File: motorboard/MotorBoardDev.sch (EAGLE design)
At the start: 88 parts, among them IC1 74HC04D, J1 Under Glow, J2 Safety Light, J3 12V, J4 24V, Q1 BC846ASMD, Q2 220mA/50V/3.5Ω, Q7 220mA/50V/3.5Ω, Q8 220mA/50V/3.5Ω, Q9 220mA/50V/3.5Ω, T11 TIP41A, T12 TIP41A, T13 TIP41A, T14 TIP41A, T15 TIP41A, T16 TIP41A, T17 TIP41A, T18 TIP41A, T19 TIP41A, T2 TIP41A, U2 9DoF IMU, X1 C-GRID-05-15-91, X2 C-GRID-05-15-91, X4 C-GRID-02-70553, X5 SI-50170, X7 2510-, X8 2510-

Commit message: restructuring
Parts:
- removed D10: WHITE, SparkFun-LED:LED0603
- removed D11, D12: 3.3V, SparkFun-DiscreteSemi:DIODE-ZENER-MM3Z3V3T1G
- removed D7: RED, SparkFun-LED:LED0603
- removed D8: BLUE, SparkFun-LED:LED0603
- removed D9: GREEN, SparkFun-LED:LED0603
- removed IC1: 74HC04D, 74xx-eu:74HC04D
- removed R20: 200, SparkFun-Resistors:200OHM-0603-1/10W-1%
- removed R26, R30: 2700, SparkFun-Resistors:3.9KOHM-0603-1/10W-1%
- removed T11, T12, T13, T14, T15, T16, T17, T18, T19: TIP41A, transistor:-PNP-TO220V
- removed U$15: MBED1768, SparkFun-Boards:MBED_NXP_LPC1768
- removed U$7: NCP1117DT50GOS-ND, IGVC-Regulators:NCP1117DT50GOS-ND
- removed U$8: NCP1117DT33GOS-ND, IGVC-Regulators:NCP1117DT33GOS-ND
- added A1: MBED1768, MotorBoardDev:SPARKFUN-BOARDS_MBED_NXP_LPC1768
- added D1, D2: GREEN, SparkFun-LED:LED-GREEN0603
- added D3: WHITE, SparkFun-LED:LED-WHITE0603
- added D4: BLUE, SparkFun-LED:LED-BLUE0603
- added FQP30N06L, Q15, Q16: TIP41C, transistor-power:TIP41C
- added Q10, Q11, Q3, Q4, Q5, Q6: TIP42C, transistor-power:TIP42C
- added T1: NCP1117DT50GOS-ND, IGVC-Regulators:NCP1117DT50GOS-ND
- added T3: NCP1117DT33GOS-ND, IGVC-Regulators:NCP1117DT33GOS-ND
- added X3: MINI-USB_SHIELD5P4-32005-400, con-cypressindustries:MINI-USB_SHIELD5P4-32005-400
- C1: device SparkFun-Capacitors:0.1UF-0603-25V-(+80/-20%) -> SparkFun-Capacitors:0.1UF-0603-100V-10%
- C11, C12, C13, C14: value (none) -> 10uF
- Q1: value BC846ASMD -> TIP42C; device transistor-npn:BC846ASMD -> transistor-power:TIP42C
- R10: value 2700 -> 200; device SparkFun-Resistors:3.9KOHM-0603-1/10W-1% -> SparkFun-Resistors:200OHM-0603-1/10W-1%
- R16: value 536 -> 200; device SparkFun-Resistors:3.9KOHM-0603-1/10W-1% -> SparkFun-Resistors:200OHM-0603-1/10W-1%
- R18, R19: value 200 -> 4.7k; device SparkFun-Resistors:200OHM-0603-1/10W-1% -> SparkFun-Resistors:4.7KOHM-0603-1/10W-1%
- R39, R40: value 150 -> 500; device rcl:R-US_R0603 -> SparkFun-Resistors:1KOHM-0603-1/10W-1%
- R7: value 200 -> 50
- R8: value 2700 -> 1800; device SparkFun-Resistors:3.9KOHM-0603-1/10W-1% -> SparkFun-Resistors:200OHM-0603-1/10W-1%
- R9: value 2700 -> 1000; device SparkFun-Resistors:3.9KOHM-0603-1/10W-1% -> SparkFun-Resistors:200OHM-0603-1/10W-1%
- T2: device transistor:-NPN-TO220V -> transistor:-PNP-TO220V
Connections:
- removed net !LDIR!: IC1C.O, R23.1
- removed net !LSPEED!: IC1D.O, R21.1
- removed net !RDIR!: IC1B.O, R24.1
- removed net !RSPEED!: IC1A.O, R22.1
- removed net N$24: D9.A, Q1.C, R17.1
- removed net N$33: D9.C, R7.2
- removed net N$34: D8.A, R10.1
- removed net N$35: D10.A, R9.1
- removed net N$7: D7.A, R8.1
- removed net SLIGHT: T2.B, U$15.P$25
- new net BLUE_OUT: J1.1, Q15.E
- new net D+: A1.P$31, X3G$1.3
- new net D-: A1.P$32, X3G$1.2
- new net GREEN_OUT: J1.2, Q16.E
- new net ID: X3G$1.4
- new net INDICATOR_LED: A1.P$8
- new net N$12: D4.A, R9.1
- new net N$5: D1.A, R5.1
- new net N$8: Q11.E, R17.1, X4-1.S
- new net RED_OUT: FQP30N06L.E, J1.3
- new net SAFETY_LIGHT: A1.P$19, T2.B
- net +12V: now also FQP30N06L.C, Q15.C, Q16.C, R17.2, R9.2, T1.IN, T3.IN; no longer R18.2, R19.2, R20.2, T11.E, T17.E, T19.E, U$7.IN, U$8.IN
- net +24V: now also R8.2; no longer D11.C, D12.C, R17.2, R30.2
- net +3V3: now also A1.P$40, R18.2, R19.2, R7.2, T3.OUT; no longer R9.2, U$8.OUT
- net +5V: now also A1.P$2, A1.P$39, R5.2, T1.OUT, X3G$1.1; no longer IC1P.VCC, U$15.P$2, U$7.OUT
- net 1S1: now also A1.P$18; no longer U$15.P$28
- net 1S1O: now also J1.7, Q1.E; no longer J1.4, T12.E
- net 1S2: now also A1.P$17; no longer U$15.P$27
- net 1S2O: now also J1.6, Q4.E; no longer J1.5, T14.E
- net 1S3: now also A1.P$16; no longer U$15.P$26
- net 1S3O: now also J1.5, Q6.E; no longer J1.6, T16.E
- net 2S1: now also A1.P$7; no longer U$15.P$5
- net 2S1O: now also Q3.E; no longer T13.E
- net 2S2: now also A1.P$6; no longer U$15.P$6
- net 2S2O: now also Q5.E; no longer T15.E
- net 2S3: now also A1.P$5; no longer U$15.P$7
- net 2S3O: now also Q10.E; no longer T18.E
- net BATTIN: now also A1.P$20, R10.1; no longer R30.1, U$15.P$20
- net BLUE: now also A1.P$21; no longer J1.1
- net ESTOP: now also A1.P$24, Q11.B; no longer R26.2, X4-1.S, X4-2.S
- net GND: now also A1.P$1, D1.C, D2.C, D3.C, D4.C, J1.4, J1.8, J1.9, J2.2, Q1.C, Q10.C, Q11.C, Q3.C, Q4.C, Q5.C, Q6.C, T1.GND, T2.C, T3.GND, X3G$1.5, X4-2.S; no longer D10.C, D7.C, D8.C, IC1P.GND, Q1.E, R26.1, R5.1, R7.1, T11.C, T12.C, T13.C, T14.C, T15.C, T16.C, T17.C, T18.C, T19.C, T2.E, U$15.P$1, U$7.GND, U$8.GND
- net GREEN: now also A1.P$22; no longer J1.2
- net GYRO_INT: now also A1.P$11; no longer U$15.P$14
- net L+12V: now also R28.2; no longer OK3A.COL, OK3B.COL, R28.1
- net LALI: now also OK3A.COL
- net LBLI: now also OK3B.COL, R28.1; no longer R28.2
- net LDIR: now also A1.P$26, R23.1; no longer IC1C.I, U$15.P$17
- net LEA3: now also A1.P$14; no longer U$15.P$24
- net LEB3: now also A1.P$15; no longer U$15.P$23
- net LSPEED: now also A1.P$25, R21.1; no longer IC1D.I, U$15.P$18
- net N$1: now also T2.E; no longer J2.2, T2.C
- net N$10: now also Q16.B; no longer R20.1, T17.B
- net N$11: now also Q6.B; no longer T16.B
- net N$13: now also Q4.B; no longer T14.B
- net N$14: now also Q1.B; no longer T12.B
- net N$15: now also Q3.B; no longer T13.B
- net N$16: now also Q5.B; no longer T15.B
- net N$28: now also Q10.B; no longer T18.B
- net N$3: now also FQP30N06L.B; no longer R18.1, T11.B
- net N$37: now also A1.P$30; no longer U$15.P$30
- net N$38: now also A1.P$29; no longer U$15.P$29
- net N$4: now also Q15.B; no longer R19.1, T19.B
- net N$6: now also D2.A, R7.1; no longer D11.A, R8.2
- net N$9: now also D3.A, R8.1; no longer D12.A, Q1.B, R5.2
- net R+12V: now also R25.2, R27.2; no longer OK4A.COL, OK4B.COL, R25.1, R27.1
- net RALI: now also OK4A.COL, R27.1; no longer R27.2
- net RBLI: now also OK4B.COL, R25.1; no longer R25.2
- net RD+: now also A1.P$35; no longer U$15.P$35
- net RD-: now also A1.P$36; no longer U$15.P$36
- net RDIR: now also A1.P$28, R24.1; no longer IC1B.I, U$15.P$15
- net REA3: now also A1.P$12; no longer U$15.P$22
- net REB3: now also A1.P$13; no longer U$15.P$21
- net RED: now also A1.P$23; no longer J1.3
- net RSPEED: now also A1.P$27, R22.1; no longer IC1A.I, U$15.P$16
- net SCL: now also A1.P$10, R18.1; no longer U$15.P$10
- net SDA: now also A1.P$9, R19.1; no longer U$15.P$9
- net TD+: now also A1.P$33; no longer U$15.P$33
- net TD-: now also A1.P$34; no longer U$15.P$34
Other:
- note added: "Also logical shifters"
- note added: "Change to AZ2940D-3.3 for assurance over power supply"
- note added: "Change to AZ2940D-5.0 for assurance over power supply"
- note added: "FQP27P06"
- note added: "How it works?"
- note added: "I'll update the package when I get the chance, they look exactly in physical layout and schematics tho"
- note added: "I'll update this when I get the chance to make the library"
- note added: "I'm not sure how 1S1O/2S1O stuff works, but I've made then at least looks functional"
- note added: "ID set to floating to identify the board as a slave"
- note added: "Inverter removed, meaning writing 255 will actually cause 0 and the other way around will cause full speed"
- note added: "Look into this"
- note added: "Overkill?"
- note added: "RGB control pin underglow thrown to PWM"
- note added: "The following are P-Channel Logic Level Mosfet, FQP27P06"
- note added: "The inverter is gone"
- note added: "These are actual logic level mosfet that can run on 3.3V, parts number: FQP30N06L"
- note added: "This is a software problem!!"
- note added: "This transistor will be FQP27P06 as well"
- note added: "Will be a connector with horizontal pinout, JST B2PS-VH"
- note added: "all of Speed control thrown to PWM"
- note added: "pull up resistor position changed, it'll no longer short L/R+12V to L/R GND"
- note removed: "Current limiting R"
- note removed: "Inverter Power"
- note removed: "Inverters"
- moved on the sheet: C1, C11, C12, C13, C14, C2, C3, C5, C6, J4, OK3A, OK3B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

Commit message: Magic
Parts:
- removed Q2, Q7, Q8, Q9: 220mA/50V/3.5Ω, SparkFun-DiscreteSemi:MOSFET-NCH-BSS138
- removed R31, R32, R33, R34, R35, R36, R37, R38: 10k, SparkFun-Resistors:10KOHM-0603-1/10W-1%
- added D5: BLUE, SparkFun-LED:LED-BLUE0603
- added U1: TXB0104DR, MotorBoardDev:TXB0104DR
- D3: value WHITE -> Yellow; device SparkFun-LED:LED-WHITE0603 -> SparkFun-LED:LED-YELLOW0603
- R10: value 200 -> 4.7k
- R16: value 200 -> 500
- R21, R22, R23, R24: value 1k -> 30
- R25, R27, R28, R29: value 10k -> 4.7k
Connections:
- net D+ renamed D_P
- net D- renamed D_N
- net RD+ renamed RD_P
- net RD- renamed RD_N
- net TD+ renamed TD_P
- net TD- renamed TD_N
- removed net ID: X3G$1.4
- removed net LSPEED: A1.P$25, R21.1
- removed net N$37: A1.P$30, R39.1
- removed net N$38: A1.P$29, R40.1
- new net LALI_CTRL: A1.P$23, R21.1
- new net LBLI_CTRL: R23.1
- new net N$17: X7-4.KL
- new net N$18: X7-3.KL
- new net N$7: J2.2, T2.E
- new net RALI_CTRL: R22.1
- new net RBLI_CTRL: R24.1
- net +3V3: now also U1.VCCB; no longer Q2.G, Q7.G, Q8.G, Q9.G, R32.2, R33.2, R35.2, R37.2
- net +5V: now also U1.VCCA; no longer R31.2, R34.2, R36.2, R38.2
- net BLUE: no longer A1.P$21
- net ESTOP: now also A1.P$22; no longer A1.P$24
- net GND: now also D5.C, U1.GND, U1.OE; no longer J1.4, J1.8, J1.9, J2.2
- net GREEN: no longer A1.P$22
- net INDICATOR_LED: now also D5.A
- net LDIR: now also A1.P$24; no longer A1.P$26, R23.1
- net LEA: now also U1.A1; no longer Q2.D, R31.1
- net LEA3: now also U1.B1; no longer Q2.S, R32.1
- net LEB: now also U1.A2; no longer Q8.D, R36.1
- net LEB3: now also U1.B2; no longer Q8.S, R37.1
- net N$1: no longer T2.E
- net RDIR: now also A1.P$26; no longer A1.P$28, R24.1
- net REA: now also U1.A3; no longer Q7.D, R34.1
- net REA3: now also U1.B3; no longer Q7.S, R33.1
- net REB: now also U1.A4; no longer Q9.D, R38.1
- net REB3: now also U1.B4; no longer Q9.S, R35.1
- net RED: no longer A1.P$23
- net RSPEED: now also A1.P$25; no longer A1.P$27, R22.1
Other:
- note added: "#S#O control which bar lights up RGB control the color of the entire stripe"
- note added: "(By OSMC Schematics"
- note added: "Add disable"
- note added: "Also make sure this is the chip we want"
- note added: "Bidirectional"
- note added: "Buck converter"
- note added: "Check 30Ω"
- note added: "Check layout package"
- note added: "If have space add Optoisolator for HI lines"
- note added: "Label them on the board"
- note added: "Make them bigger"
- note added: "Power distribution load switch"
- note added: "Put it bak on"
- note added: "RGB are currently not connected to the mbed"
- note added: "Use Neopixels"
- note added: "Use quad-line 12V inverter"
- note added: "also goes for this"
- note added: "do the same for safety light"
- note added: "fix this"
- note added: "get a SMD?"
- note added: "go from 5v to 3v3 not 12V"
- note added: "make absolute voltage 3V"
- note removed: "Also logical shifters"
- note removed: "How it works?"
- note removed: "ID set to floating to identify the board as a slave"
- note removed: "Inverter removed, meaning writing 255 will actually cause 0 and the other way around will cause full speed"
- note removed: "Overkill?"
- note removed: "RGB control pin underglow thrown to PWM"
- note removed: "This is a software problem!!"
- note removed: "all of Speed control thrown to PWM"
- note removed: "pull up resistor position changed, it'll no longer short L/R+12V to L/R GND"
- moved on the sheet: C3, C4, OK3A, OK4A, OK4B, Q15, Q16, R18, R19, R2, R21, R22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

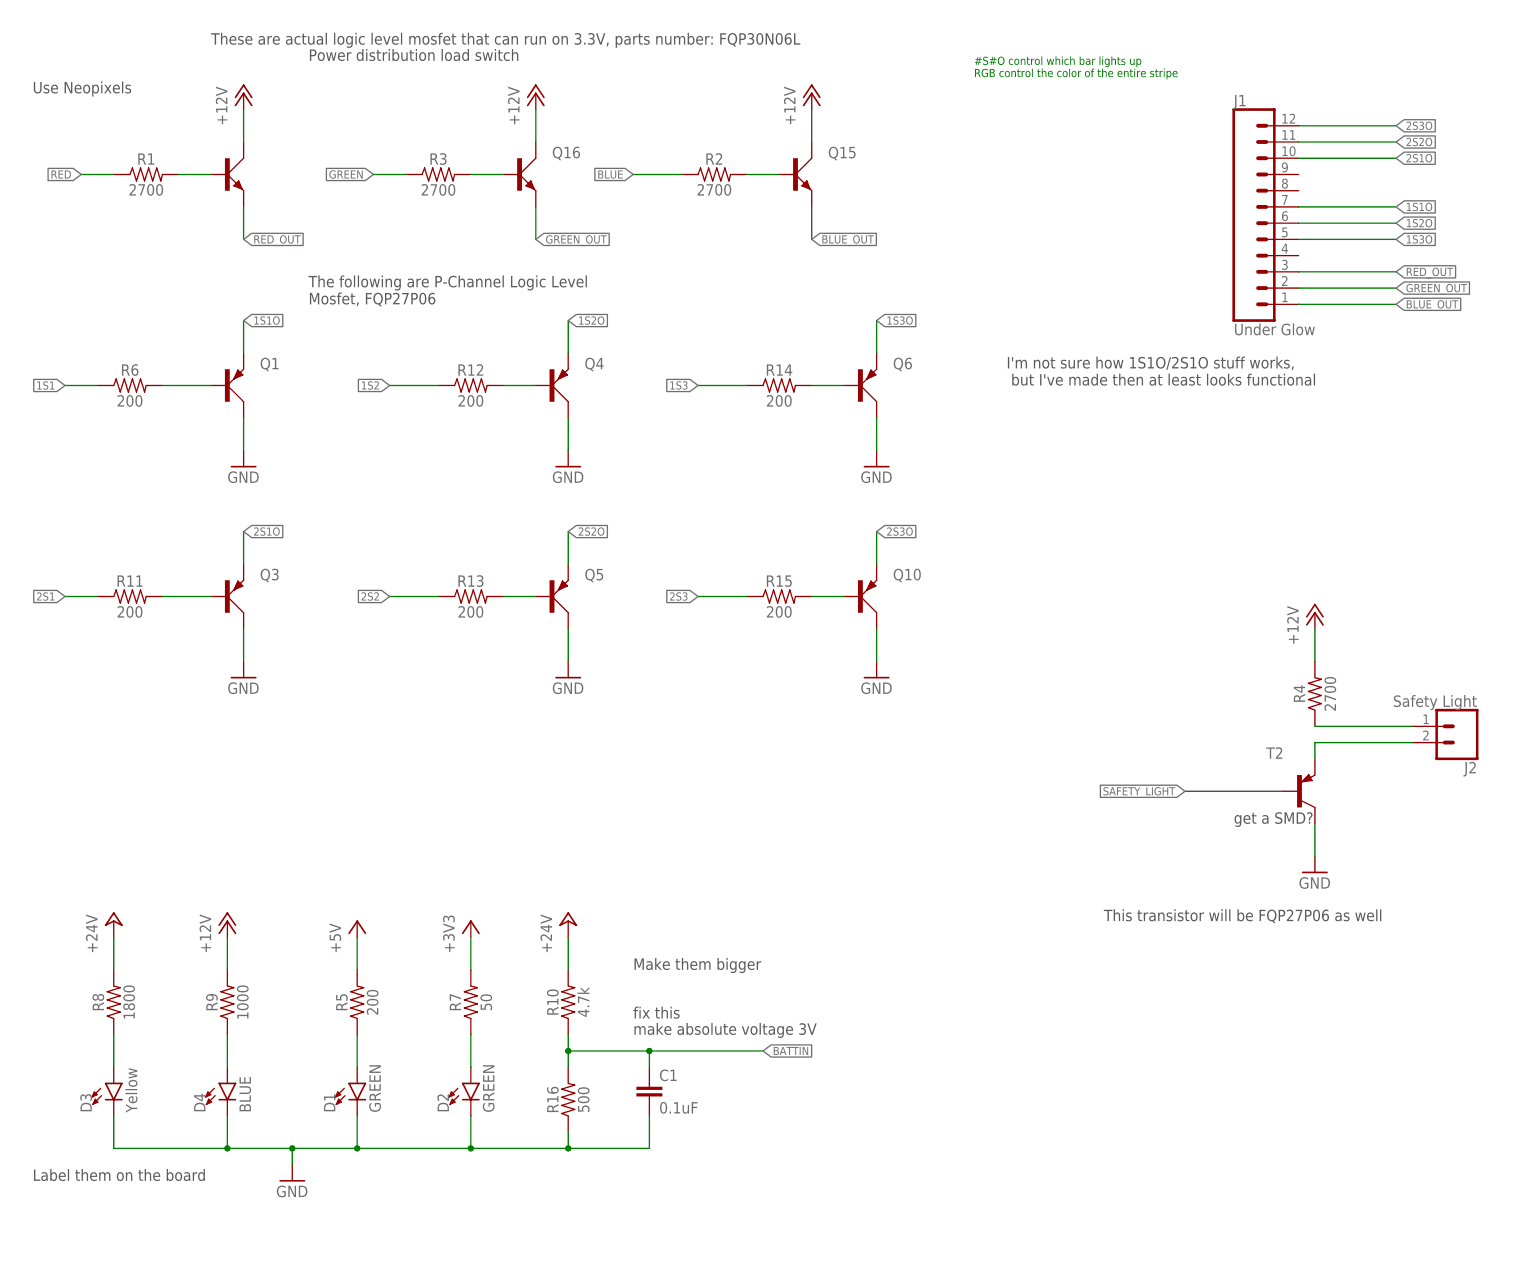
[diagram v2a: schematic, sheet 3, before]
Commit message: Changes so far so Ryan3 can complete BOM
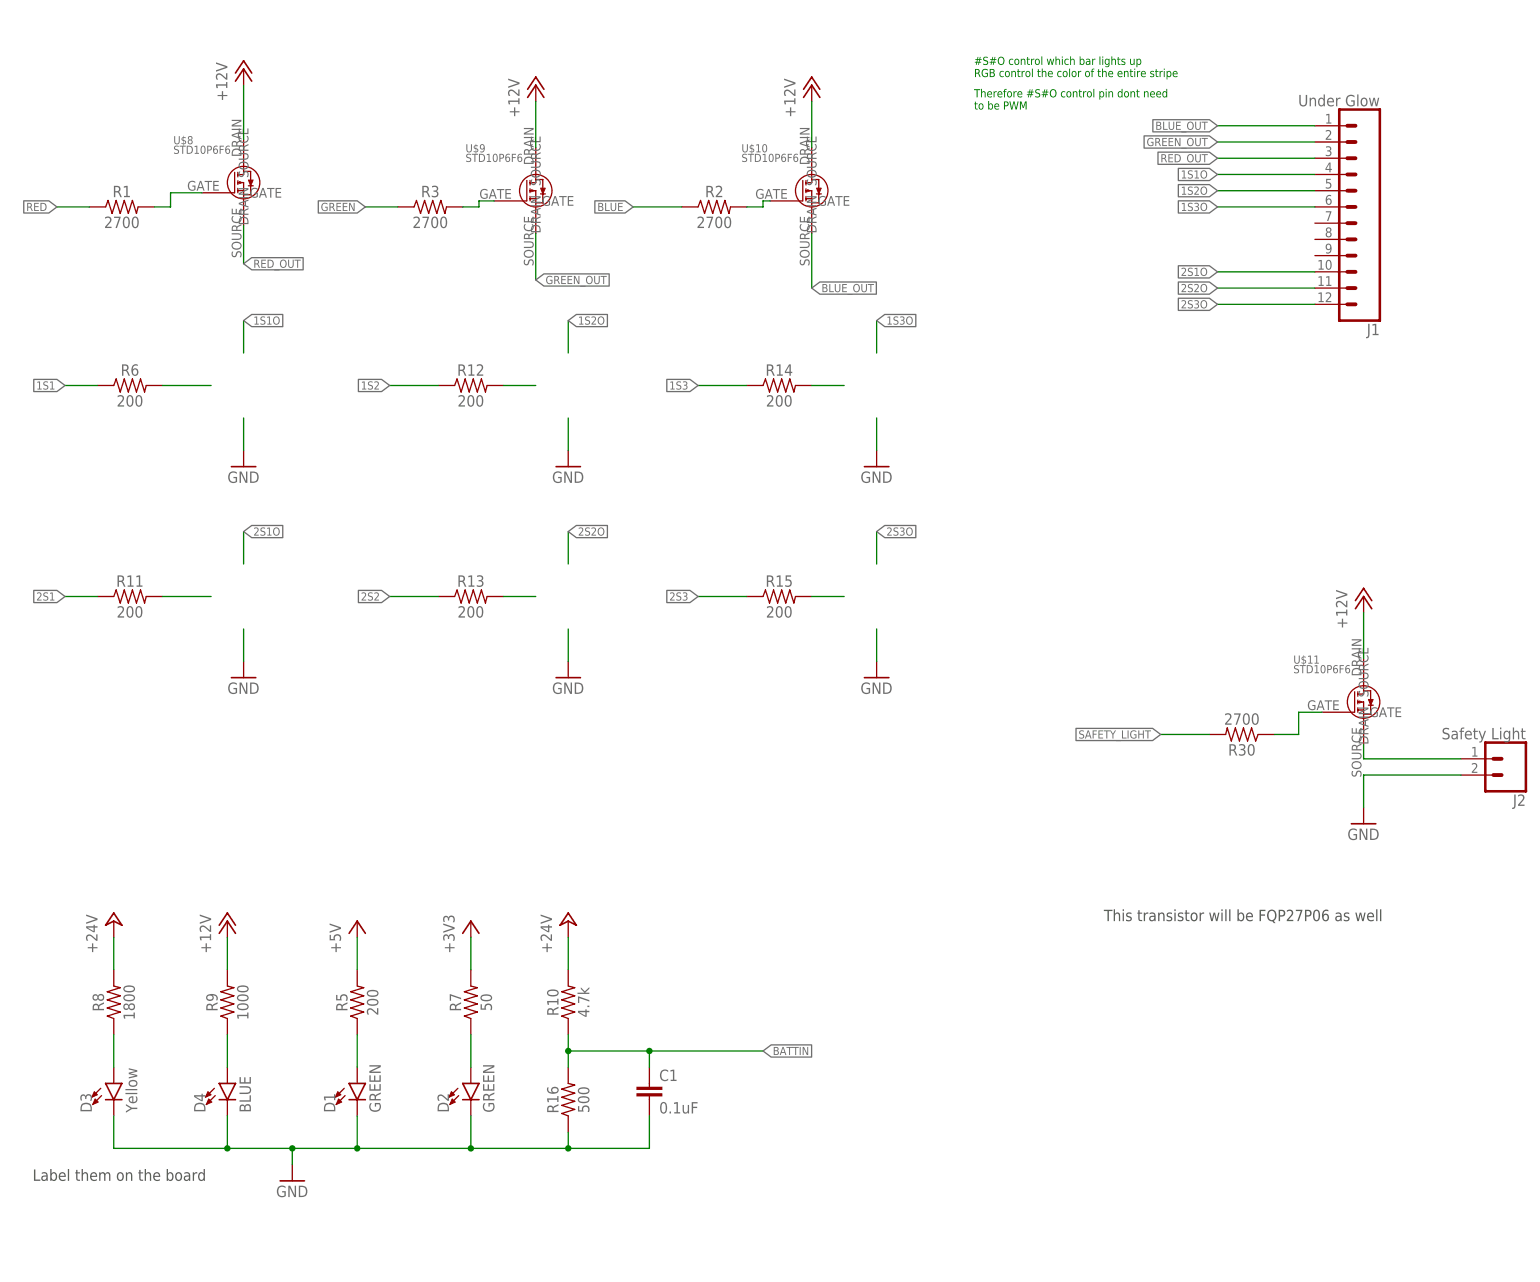
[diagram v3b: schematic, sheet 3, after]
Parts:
- removed FQP30N06L, Q15, Q16: TIP41C, transistor-power:TIP41C
- removed Q1, Q10, Q11, Q3, Q4, Q5, Q6: TIP42C, transistor-power:TIP42C
- removed R17: 2700, SparkFun-Resistors:3.9KOHM-0603-1/10W-1%
- removed T2: TIP41A, transistor:-PNP-TO220V
- added R20, R26: 1k, SparkFun-Resistors:10KOHM-0603-1/10W-1%
- added R30: 2700, SparkFun-Resistors:3.9KOHM-0603-1/10W-1%
- added U$10, U$11, U$12, U$8, U$9: STD10P6F6, MotorBoardDev:STD10P6F6
- added U3, U4: TXB0104DR, MotorBoardDev:TXB0104DR
- R4: value 2700 -> (none); device SparkFun-Resistors:3.9KOHM-0603-1/10W-1% -> rcl:R-US_R0603
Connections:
- removed net LDIR: A1.P$24
- removed net RDIR: A1.P$26
- removed net RSPEED: A1.P$25
- new net LDISABLE: R20.2, X7-4.KL
- new net N$19: R3.2, U$9.GATE
- new net RDISABLE: R26.2, X8-4.KL
- net +12V: now also U$10.DRAIN, U$11.DRAIN, U$12.DRAIN, U$8.DRAIN, U$9.DRAIN; no longer FQP30N06L.C, Q15.C, Q16.C, R17.2, R4.2
- net 1S1O: now also J1.4; no longer J1.7, Q1.E
- net 1S2O: now also J1.5; no longer J1.6, Q4.E
- net 1S3O: now also J1.6; no longer J1.5, Q6.E
- net 2S1O: no longer Q3.E
- net 2S2O: no longer Q5.E
- net 2S3O: no longer Q10.E
- net BLUE: now also A1.P$29
- net BLUE_OUT: now also U$10.SOURCE; no longer Q15.E
- net ESTOP: now also A1.P$27, R4.1; no longer A1.P$22, Q11.B
- net GND: now also J2.2; no longer Q1.C, Q10.C, Q11.C, Q3.C, Q4.C, Q5.C, Q6.C, T2.C
- net GREEN: now also A1.P$28
- net GREEN_OUT: now also U$9.SOURCE; no longer Q16.E
- net LBLI_CTRL: now also A1.P$24
- net LGND: now also R20.1
- net N$1: now also U$11.SOURCE; no longer R4.1
- net N$10: now also U$12.SOURCE, X4-1.S; no longer Q16.B, R3.2
- net N$11: no longer Q6.B
- net N$13: no longer Q4.B
- net N$14: no longer Q1.B
- net N$15: no longer Q3.B
- net N$16: no longer Q5.B
- net N$17: now also A1.P$22, R39.1; no longer X7-4.KL
- net N$18: now also A1.P$21, R40.1; no longer X7-3.KL
- net N$28: no longer Q10.B
- net N$3: now also U$8.GATE; no longer FQP30N06L.B
- net N$4: now also U$10.GATE; no longer Q15.B
- net N$7: now also R30.1, U$11.GATE; no longer J2.2, T2.E
- net N$8: now also R4.2, U$12.GATE; no longer Q11.E, R17.1, X4-1.S
- net RALI_CTRL: now also A1.P$25
- net RBLI_CTRL: now also A1.P$26
- net RED: now also A1.P$30
- net RED_OUT: now also U$8.SOURCE; no longer FQP30N06L.E
- net RGND: now also R26.1
- net SAFETY_LIGHT: now also R30.2; no longer T2.B
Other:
- note added: "Checked, both device and package"
- note added: "Input Current 200mA Voltage 5V \therefore R = 25Ω ish"
- note added: "No we dont"
- note added: "RGB are currently connected to normal digital pins"
- note added: "Review the connection of DISABLE"
- note added: "Therefore #S#O control pin dont need to be PWM"
- note added: "Third pin points to Battery voltage level, something we already have, see battery sensor/Status Light, so not using it"
- note removed: "(By OSMC Schematics"
- note removed: "Add disable"
- note removed: "Also make sure this is the chip we want"
- note removed: "Check 30Ω"
- note removed: "Check layout package"
- note removed: "FQP27P06"
- note removed: "I'm not sure how 1S1O/2S1O stuff works, but I've made then at least looks functional"
- note removed: "Look into this"
- note removed: "Make them bigger"
- note removed: "Power distribution load switch"
- note removed: "RGB are currently not connected to the mbed"
- note removed: "The following are P-Channel Logic Level Mosfet, FQP27P06"
- note removed: "These are actual logic level mosfet that can run on 3.3V, parts number: FQP30N06L"
- note removed: "Use Neopixels"
- note removed: "Use quad-line 12V inverter"
- note removed: "also goes for this"
- note removed: "do the same for safety light"
- note removed: "fix this"
- note removed: "get a SMD?"
- note removed: "make absolute voltage 3V"
- moved on the sheet: J1, J2, R1, R2, R3, R39, R40
